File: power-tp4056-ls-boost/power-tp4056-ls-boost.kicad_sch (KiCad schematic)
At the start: 32 parts, among them J0 USB_C_Receptacle_PowerOnly_6P, J1 Conn_01x01, J2 Conn_01x01, J3 Conn_01x01, J4 Conn_01x01, J5 Conn_01x01, J6 Conn_01x01, Q1 AO3401A, Q2 AO3401A, SW1 SW_SPDT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

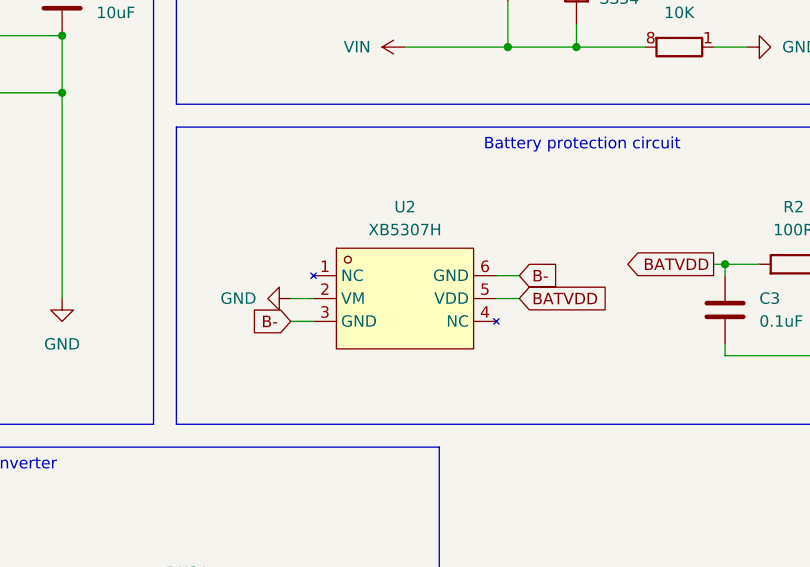
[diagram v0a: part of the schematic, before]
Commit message: Replace XB5307H with XB5350D0 for Li-Ion battery protection
XB5307H has an overcharge cutoff voltage of 4.425V, while XB5350D0 has
an overcharge cutoff voltage of 4.25V. Both ICs have an underdischarge
cutoff voltage of 3V.
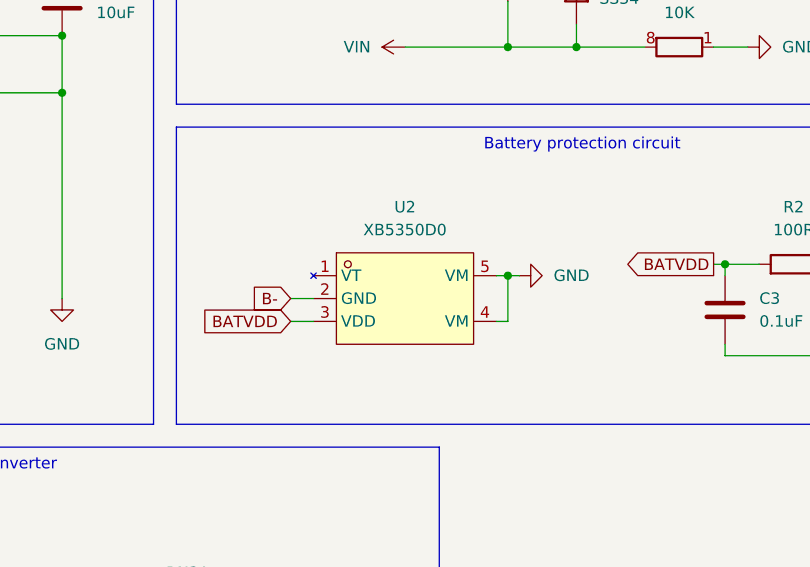
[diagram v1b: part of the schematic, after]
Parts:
- U2: value XB5307H -> XB5350D0; footprint Package_TO_SOT_SMD:SOT-23-6_Handsoldering -> custom:SOT-23-5_simple; symbol lcsc:XB5307H -> lcsc:XB5350D0; LCSC Part C154942 -> C2760002
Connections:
- net B-: now also U2.2 (GND); no longer U2.3 (GND), U2.6 (GND)
- net BATVDD: now also U2.3 (VDD); no longer U2.5 (VDD)
- net GND: now also U2.4 (VM), U2.5 (VM); no longer U2.2 (VM)
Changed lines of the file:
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@@
 	)
 	(junction
+		(at 228.6 67.31)
+		(diameter 0)
+		(color 0 0 0 0)
+	)
+	(junction
 		(at 228.6 41.91)
 		(diameter 0)
@@
 	(wire
 		(pts
+			(xy 228.6 72.39) (xy 228.6 67.31)
+		)
+		(stroke
+			(width 0)
+			(type default)
+		)
+	)
+	(wire
+		(pts
 			(xy 176.53 121.92) (xy 180.34 121.92)
 		)
@@
 	(wire
 		(pts
-			(xy 229.87 67.31) (xy 227.33 67.31)
+			(xy 229.87 67.31) (xy 228.6 67.31)
 		)
 		(stroke
@@
 	(wire
 		(pts
-			(xy 229.87 69.85) (xy 227.33 69.85)
+			(xy 52.07 31.75) (xy 64.77 31.75)
 		)
 		(stroke
@@
 	(wire
 		(pts
-			(xy 52.07 31.75) (xy 64.77 31.75)
+			(xy 146.05 67.31) (xy 146.05 69.85)
 		)
 		(stroke
@@
 	(wire
 		(pts
-			(xy 146.05 67.31) (xy 146.05 69.85)
+			(xy 36.83 57.15) (xy 36.83 59.69)
 		)
 		(stroke
@@
 	(wire
 		(pts
-			(xy 36.83 57.15) (xy 36.83 59.69)
+			(xy 52.07 44.45) (xy 64.77 44.45)
 		)
 		(stroke
@@
 	(wire
 		(pts
-			(xy 52.07 44.45) (xy 64.77 44.45)
+			(xy 204.47 69.85) (xy 207.01 69.85)
 		)
 		(stroke
@@
 	(wire
 		(pts
-			(xy 204.47 69.85) (xy 207.01 69.85)
+			(xy 29.21 59.69) (xy 36.83 59.69)
 		)
 		(stroke
@@
 	(wire
 		(pts
-			(xy 29.21 59.69) (xy 36.83 59.69)
+			(xy 227.33 72.39) (xy 228.6 72.39)
 		)
 		(stroke
@@
 	(wire
 		(pts
+			(xy 228.6 67.31) (xy 227.33 67.31)
+		)
+		(stroke
+			(width 0)
+			(type default)
+		)
+	)
+	(wire
+		(pts
 			(xy 127 46.99) (xy 130.81 46.99)
 		)
@@
 	(global_label "B-"
 		(shape input)
-		(at 229.87 67.31 0)
+		(at 204.47 69.85 180)
 		(fields_autoplaced yes)
 		(effects
@@
 				(size 1.27 1.27)
 			)
-			(justify left)
+			(justify right)
 		)
 		(property "Intersheetrefs" "${INTERSHEET_REFS}"
-			(at 235.6976 67.31 0)
+			(at 198.6424 69.85 0)
 			(effects
 				(font
 					(size 1.27 1.27)
 				)
-				(justify left)
+				(justify right)
+				(hide yes)
+			)
+		)
+	)
+	(global_label "BATVDD"
+		(shape input)
+		(at 204.47 72.39 180)
+		(fields_autoplaced yes)
+		(effects
+			(font
+				(size 1.27 1.27)
+			)
+			(justify right)
+		)
+		(property "Intersheetrefs" "${INTERSHEET_REFS}"
+			(at 194.53 72.39 0)
+			(effects
+				(font
+					(size 1.27 1.27)
+				)
+				(justify right)
 				(hide yes)
 			)
@@
 		)
 	)
-	(global_label "B-"
-		(shape input)
-		(at 204.47 72.39 180)
-		(fields_autoplaced yes)
-		(effects
-			(font
-				(size 1.27 1.27)
-			)
-			(justify right)
-		)
-		(property "Intersheetrefs" "${INTERSHEET_REFS}"
-			(at 198.6424 72.39 0)
-			(effects
-				(font
-					(size 1.27 1.27)
-				)
-				(justify right)
-				(hide yes)
-			)
-		)
-	)
 	(global_label "BATVDD"
 		(shape output)
@@
 		)
 	)
-	(global_label "BATVDD"
-		(shape input)
-		(at 229.87 69.85 0)
-		(fields_autoplaced yes)
-		(effects
-			(font
-				(size 1.27 1.27)
-			)
-			(justify left)
-		)
-		(property "Intersheetrefs" "${INTERSHEET_REFS}"
-			(at 239.81 69.85 0)
-			(effects
-				(font
-					(size 1.27 1.27)
-				)
-				(justify left)
-				(hide yes)
-			)
-		)
-	)
 	(symbol
 		(lib_id "power:GND")
@@
 	)
 	(symbol
-		(lib_id "lcsc:XB5307H")
+		(lib_id "lcsc:XB5350D0")
 		(at 217.17 69.85 0)
 		(unit 1)
@@
 			)
 		)
-		(property "Value" "XB5307H"
+		(property "Value" "XB5350D0"
 			(at 217.17 62.23 0)
 			(effects
@@
 			)
 		)
-		(property "Footprint" "Package_TO_SOT_SMD:SOT-23-6_Handsoldering"
+		(property "Footprint" "custom:SOT-23-5_simple"
 			(at 217.17 80.01 0)
 			(effects
@@
 		)
 		(property "Datasheet" "https://lcsc.com/product-detail/Battery-Protection-ICs_XB5307H_C154942.html"
-			(at 217.17 82.55 0)
+			(at 217.17 69.85 0)
 			(effects
 				(font
@@
 			)
 		)
-		(property "LCSC Part" "C154942"
-			(at 217.17 85.09 0)
+		(property "LCSC Part" "C2760002"
+			(at 217.17 82.55 0)
 			(effects
 				(font
@@
 		(pin "2"
 		)
-		(pin "6"
-		)
 		(pin "1"
 		)
@@
 	)
 	(symbol
+		(lib_id "power:GND")
+		(at 229.87 67.31 90)
+		(unit 1)
+		(exclude_from_sim no)
+		(in_bom yes)
+		(on_board yes)
+		(dnp no)
+		(fields_autoplaced yes)
+		(property "Reference" "#PWR021"
+			(at 236.22 67.31 0)
+			(effects
+				(font
+					(size 1.27 1.27)
+				)
+				(hide yes)
+			)
+		)
+		(property "Value" "GND"
+			(at 233.68 67.3099 90)
+			(effects
+				(font
+					(size 1.27 1.27)
+				)
+				(justify right)
+			)
+		)
+		(property "Footprint" ""
+			(at 229.87 67.31 0)
+			(effects
+				(font
+					(size 1.27 1.27)
+				)
+				(hide yes)
+			)
+		)
+		(property "Datasheet" ""
+			(at 229.87 67.31 0)
+			(effects
+				(font
+					(size 1.27 1.27)
+				)
+				(hide yes)
+			)
+		)
+		(property "Description" "Power symbol creates a global label with name \"GND\" , ground"
+			(at 229.87 67.31 0)
+			(effects
+				(font
+					(size 1.27 1.27)
+				)
+				(hide yes)
+			)
+		)
+		(pin "1"
+		)
+		(instances
+			(project "power-tp4056-ls-boost"
+				(path "/f7334e40-25a3-4306-9a4a-47752c843a90"
+					(reference "#PWR021")
+					(unit 1)
+				)
+			)
+		)
+	)
+	(symbol
 		(lib_id "Device:R_Pack04_Split")
 		(at 193.04 106.68 270)
@@
 				)
 			)
-		)
-	)
-	(symbol
-		(lib_id "power:GND")
-		(at 204.47 69.85 270)
-		(unit 1)
-		(exclude_from_sim no)
-		(in_bom yes)
-		(on_board yes)
-		(dnp no)
-		(fields_autoplaced yes)
-		(property "Reference" "#PWR021"
-			(at 198.12 69.85 0)
-			(effects
-				(font
-					(size 1.27 1.27)
-				)
-				(hide yes)
-			)
-		)
-		(property "Value" "GND"
-			(at 200.66 69.8499 90)
-			(effects
-				(font
-					(size 1.27 1.27)
-				)
-				(justify right)
-			)
-		)
-		(property "Footprint" ""
-			(at 204.47 69.85 0)
-			(effects
-				(font
-					(size 1.27 1.27)
-				)
-				(hide yes)
-			)
-		)
-		(property "Datasheet" ""
-			(at 204.47 69.85 0)
-			(effects
-				(font
-					(size 1.27 1.27)
-				)
-				(hide yes)
-			)
-		)
-		(property "Description" "Power symbol creates a global label with name \"GND\" , ground"
-			(at 204.47 69.85 0)
-			(effects
-				(font
-					(size 1.27 1.27)
-				)
-				(hide yes)
-			)
-		)
-		(pin "1"
-		)
-		(instances
-			(project "power-tp4056-ls-boost"
-				(path "/f7334e40-25a3-4306-9a4a-47752c843a90"
-					(reference "#PWR021")
-					(unit 1)
-				)
-			)
